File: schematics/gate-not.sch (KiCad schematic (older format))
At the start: 3 parts, among them Q13 NPN

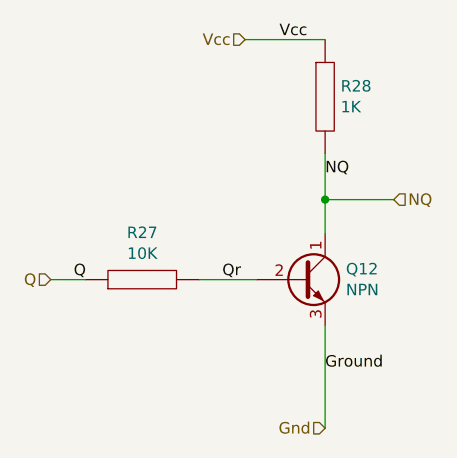
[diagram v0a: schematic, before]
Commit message: ALU is sketched but has functional defects
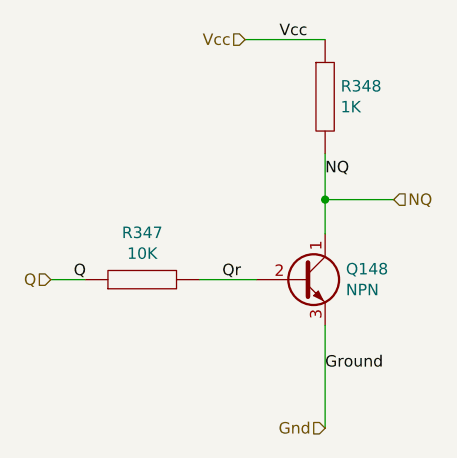
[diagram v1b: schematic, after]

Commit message: Adds a netlist "optimizer" which shortens names for better output parsing
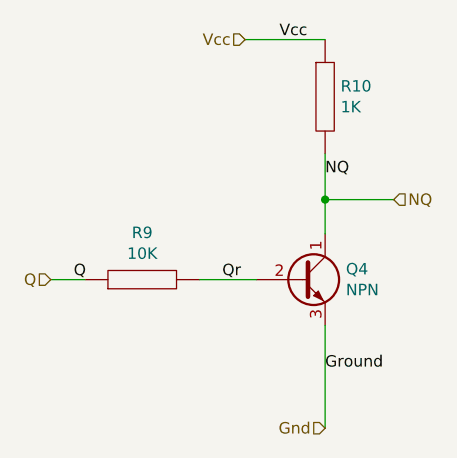
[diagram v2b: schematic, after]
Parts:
- renumbered Q13 to Q3, R37 to R7, R38 to R8

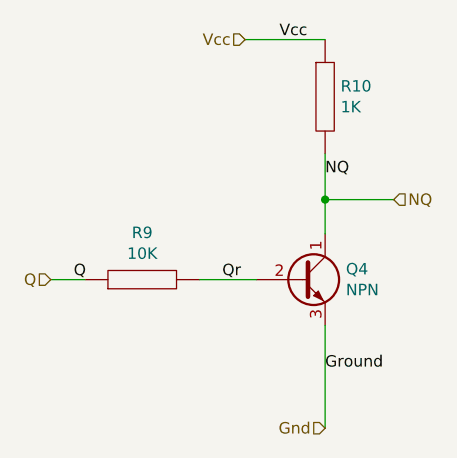
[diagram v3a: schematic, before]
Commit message: Adds some tests for and-2, nor-2, nor-3
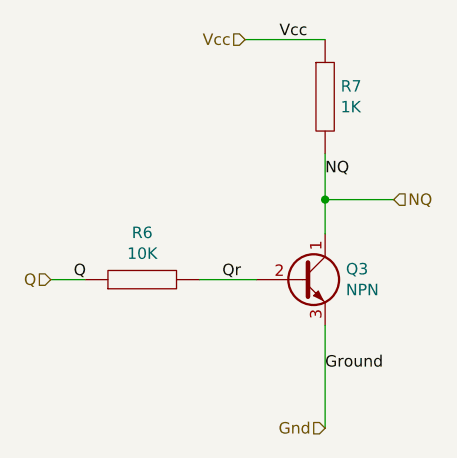
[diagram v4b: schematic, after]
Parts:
- renumbered Q3 to Q2, R7 to R4, R8 to R5
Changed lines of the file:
@@
 EESchema Schematic File Version 4
-LIBS:gate-not-test-cache
+LIBS:gate-and-2-test-cache
 EELAYER 26 0
 EELAYER END
 $Descr A4 11693 8268
 encoding utf-8
-Sheet 76 2
+Sheet 76 5
 Title ""
 Date ""
@@
 AR Path="/5C4EA7CD/5C4EE0DF/5C4501B1/5C443DB5/5C3FFE07/5C561AAC/5C561AAF" Ref="R?"  Part="1"
 AR Path="/5C4EA7CD/5C4EE0DF/5C4501B1/5C443DB5/5C3FFE07/5C561AB4/5C561AAF" Ref="R?"  Part="1"
-AR Path="/5C4DE58B/5C4DE6C4/5C561AAC/5C561AAF" Ref="R8"  Part="1"
-AR Path="/5C4DE58B/5C4DE6C4/5C561AB4/5C561AAF" Ref="R10"  Part="1"
-F 0 "R10" H 5068 3246 50  0000 L CNN
+AR Path="/5C4DE58B/5C4DE6C4/5C561AAC/5C561AAF" Ref="R?"  Part="1"
+AR Path="/5C4DE58B/5C4DE6C4/5C561AB4/5C561AAF" Ref="R?"  Part="1"
+AR Path="/5C3FE316/5C561AAC/5C561AAF" Ref="R5"  Part="1"
+AR Path="/5C3FE316/5C561AB4/5C561AAF" Ref="R7"  Part="1"
+F 0 "R7" H 5068 3246 50  0000 L CNN
 F 1 "1K" H 5068 3155 50  0000 L CNN
 F 2 "" H 5000 3200 50  0001 C CNN
@@
 AR Path="/5C4EA7CD/5C4EE0DF/5C4501B1/5C443DB5/5C3FFE07/5C561AAC/5C561AB2" Ref="R?"  Part="1"
 AR Path="/5C4EA7CD/5C4EE0DF/5C4501B1/5C443DB5/5C3FFE07/5C561AB4/5C561AB2" Ref="R?"  Part="1"
-AR Path="/5C4DE58B/5C4DE6C4/5C561AAC/5C561AB2" Ref="R7"  Part="1"
-AR Path="/5C4DE58B/5C4DE6C4/5C561AB4/5C561AB2" Ref="R9"  Part="1"
-F 0 "R9" V 4405 4000 50  0000 C CNN
+AR Path="/5C4DE58B/5C4DE6C4/5C561AAC/5C561AB2" Ref="R?"  Part="1"
+AR Path="/5C4DE58B/5C4DE6C4/5C561AB4/5C561AB2" Ref="R?"  Part="1"
+AR Path="/5C3FE316/5C561AAC/5C561AB2" Ref="R4"  Part="1"
+AR Path="/5C3FE316/5C561AB4/5C561AB2" Ref="R6"  Part="1"
+F 0 "R6" V 4405 4000 50  0000 C CNN
 F 1 "10K" V 4314 4000 50  0000 C CNN
 F 2 "" H 4200 4000 50  0001 C CNN
@@
 AR Path="/5C4EA7CD/5C4EE0DF/5C4501B1/5C443DB5/5C3FFE07/5C561AAC/5C561ABA" Ref="Q?"  Part="1"
 AR Path="/5C4EA7CD/5C4EE0DF/5C4501B1/5C443DB5/5C3FFE07/5C561AB4/5C561ABA" Ref="Q?"  Part="1"
-AR Path="/5C4DE58B/5C4DE6C4/5C561AAC/5C561ABA" Ref="Q3"  Part="1"
-AR Path="/5C4DE58B/5C4DE6C4/5C561AB4/5C561ABA" Ref="Q4"  Part="1"
-F 0 "Q4" H 5091 4046 50  0000 L CNN
+AR Path="/5C4DE58B/5C4DE6C4/5C561AAC/5C561ABA" Ref="Q?"  Part="1"
+AR Path="/5C4DE58B/5C4DE6C4/5C561AB4/5C561ABA" Ref="Q?"  Part="1"
+AR Path="/5C3FE316/5C561AAC/5C561ABA" Ref="Q2"  Part="1"
+AR Path="/5C3FE316/5C561AB4/5C561ABA" Ref="Q3"  Part="1"
+F 0 "Q3" H 5091 4046 50  0000 L CNN
 F 1 "NPN" H 5091 3955 50  0000 L CNN
 F 2 "Package_TO_SOT_THT:TO-92_Inline" H 5100 3925 50  0001 L CIN

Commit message: Test output is a bit more functional... ALU still has defects
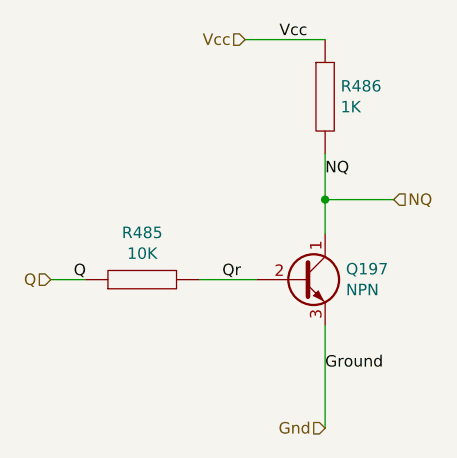
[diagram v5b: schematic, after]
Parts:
- renumbered Q2 to Q41, R4 to R97, R5 to R98

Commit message: ALU appears to work as expected
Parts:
- renumbered R98 to R97, R97 to R98
